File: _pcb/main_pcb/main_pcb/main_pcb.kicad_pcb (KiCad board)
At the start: 2 copper layers, 160 x 110 mm, 6 parts, among them U1 Pico, U2 74HC4051

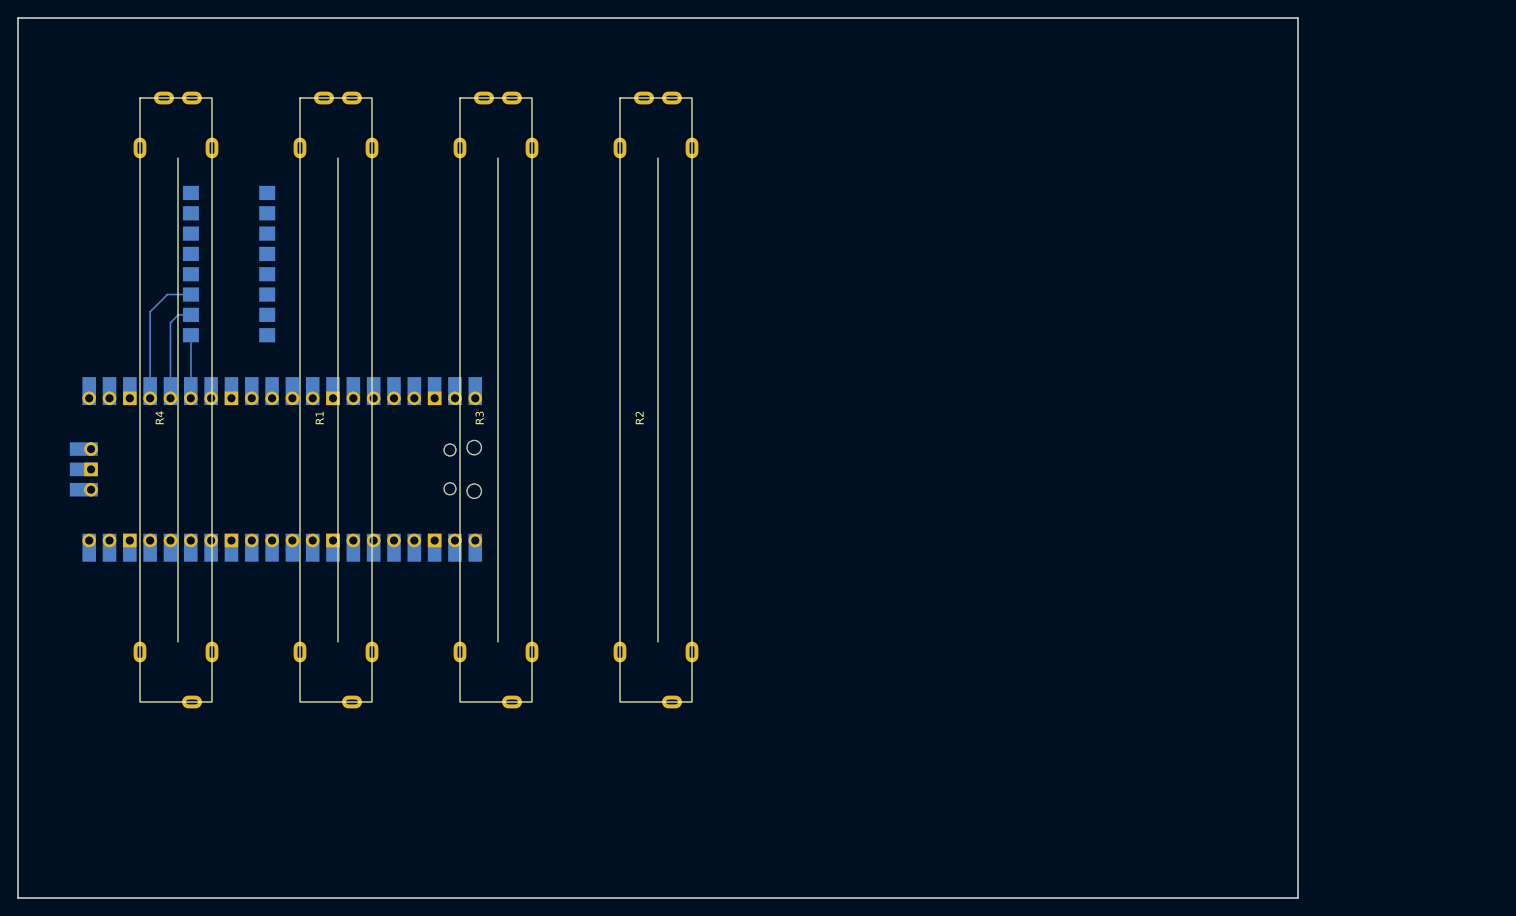
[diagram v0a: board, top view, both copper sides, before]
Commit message: for now the last commit for pcb as buying pcb is too expensive
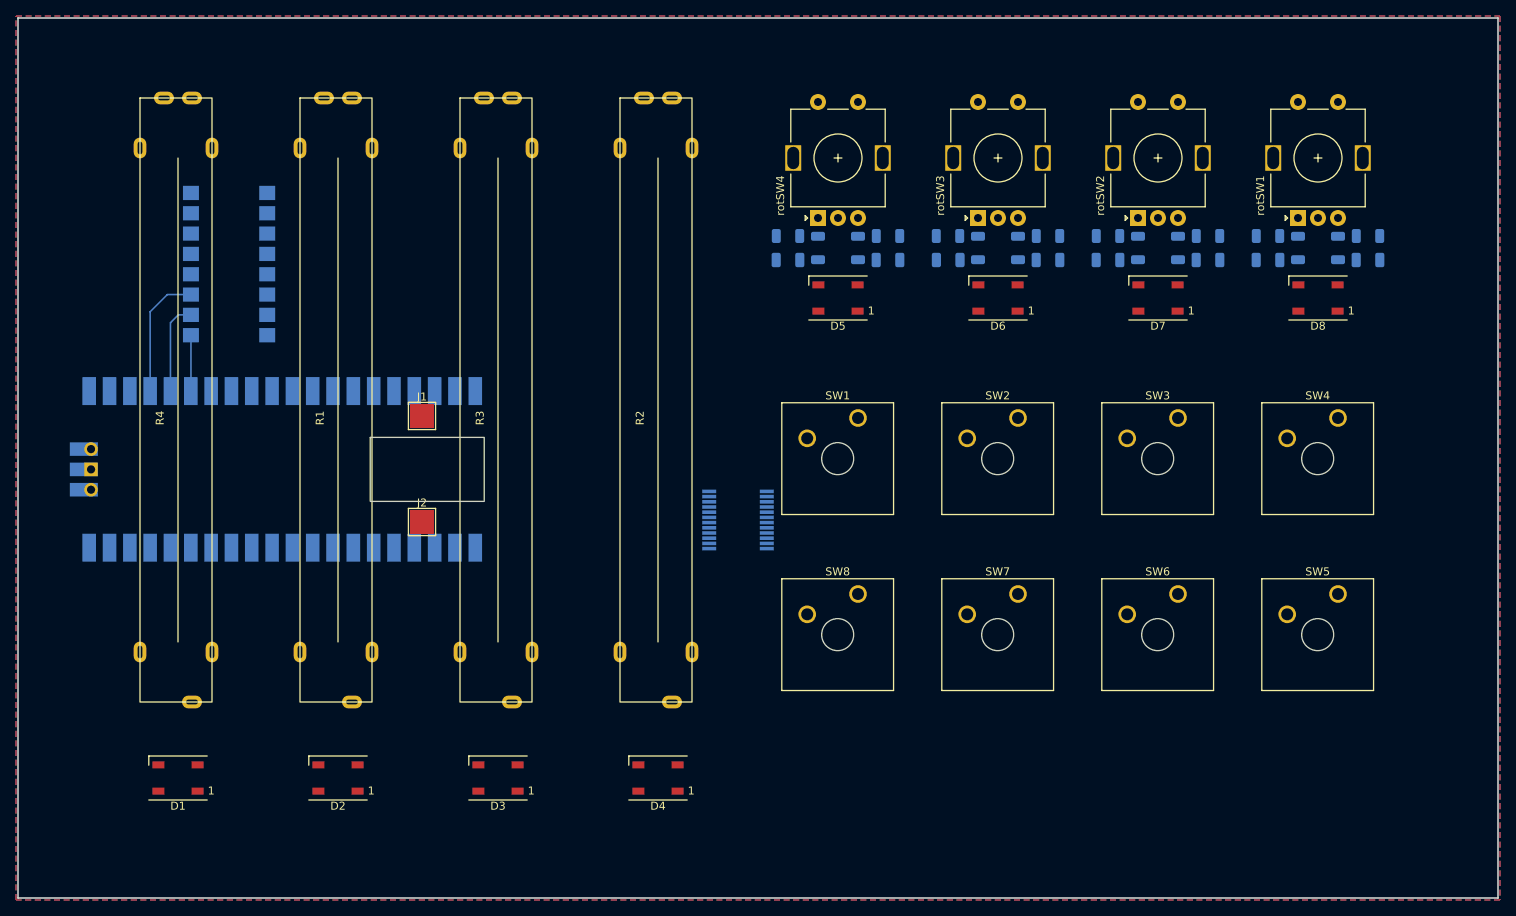
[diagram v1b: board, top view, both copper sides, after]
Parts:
- added C1: C, Capacitor_SMD:C_1206_3216Metric, B.Cu at (188.8, 80.2)
- added C2: C, Capacitor_SMD:C_1206_3216Metric, B.Cu at (176.2, 80.2)
- added C3: C, Capacitor_SMD:C_1206_3216Metric, B.Cu at (156.2, 80.2)
- added C4: C, Capacitor_SMD:C_1206_3216Metric, B.Cu at (168.8, 80.2)
- added C5: C, Capacitor_SMD:C_1206_3216Metric, B.Cu at (136.3, 80.2)
- added C6: C, Capacitor_SMD:C_1206_3216Metric, B.Cu at (148.8, 80.2)
- added C7: C, Capacitor_SMD:C_1206_3216Metric, B.Cu at (116.2, 80.2)
- added C8: C, Capacitor_SMD:C_1206_3216Metric, B.Cu at (128.8, 80.2)
- added D1: WS2812B, LED_SMD:LED_WS2812B_PLCC4_5.0x5.0mm_P3.2mm, F.Cu at (40.0, 145.0)
- added D2: WS2812B, LED_SMD:LED_WS2812B_PLCC4_5.0x5.0mm_P3.2mm, F.Cu at (60.0, 145.0)
- added D3: WS2812B, LED_SMD:LED_WS2812B_PLCC4_5.0x5.0mm_P3.2mm, F.Cu at (80.0, 145.0)
- added D4: WS2812B, LED_SMD:LED_WS2812B_PLCC4_5.0x5.0mm_P3.2mm, F.Cu at (100.0, 145.0)
- added D5: WS2812B, LED_SMD:LED_WS2812B_PLCC4_5.0x5.0mm_P3.2mm, F.Cu at (122.5, 85.0)
- added D6: WS2812B, LED_SMD:LED_WS2812B_PLCC4_5.0x5.0mm_P3.2mm, F.Cu at (142.5, 85.0)
- added D7: WS2812B, LED_SMD:LED_WS2812B_PLCC4_5.0x5.0mm_P3.2mm, F.Cu at (162.5, 85.0)
- added D8: WS2812B, LED_SMD:LED_WS2812B_PLCC4_5.0x5.0mm_P3.2mm, F.Cu at (182.5, 85.0)
- added J1: Conn_01x01_Pin, TestPoint:TestPoint_Pad_3.0x3.0mm, F.Cu at (70.5, 99.8)
- added J2: Conn_01x01_Pin, TestPoint:TestPoint_Pad_3.0x3.0mm, F.Cu at (70.5, 113.0)
- added R10: R, Resistor_SMD:R_1206_3216Metric, B.Cu at (165.0, 78.8)
- added R11: R, Resistor_SMD:R_1206_3216Metric, B.Cu at (156.2, 77.2)
- added R12: R, Resistor_SMD:R_1206_3216Metric, B.Cu at (168.8, 77.2)
- added R13: R, Resistor_SMD:R_1206_3216Metric, B.Cu at (140.0, 78.8)
- added R14: R, Resistor_SMD:R_1206_3216Metric, B.Cu at (145.0, 78.8)
- added R15: R, Resistor_SMD:R_1206_3216Metric, B.Cu at (136.2, 77.2)
- added R16: R, Resistor_SMD:R_1206_3216Metric, B.Cu at (148.8, 77.2)
- added R17: R, Resistor_SMD:R_1206_3216Metric, B.Cu at (120.0, 78.8)
- added R18: R, Resistor_SMD:R_1206_3216Metric, B.Cu at (125.0, 78.8)
- added R19: R, Resistor_SMD:R_1206_3216Metric, B.Cu at (116.2, 77.2)
- added R20: R, Resistor_SMD:R_1206_3216Metric, B.Cu at (128.8, 77.2)
- added R5: R, Resistor_SMD:R_1206_3216Metric, B.Cu at (185.0, 78.8)
- added R6: R, Resistor_SMD:R_1206_3216Metric, B.Cu at (180.0, 78.8)
- added R7: R, Resistor_SMD:R_1206_3216Metric, B.Cu at (176.2, 77.2)
- added R8: R, Resistor_SMD:R_1206_3216Metric, B.Cu at (188.8, 77.2)
- added R9: R, Resistor_SMD:R_1206_3216Metric, B.Cu at (160.0, 78.8)
- added SW1: SW_Push, Button_Switch_Keyboard:SW_Cherry_MX_1.00u_Plate, F.Cu at (125.0, 100.0)
- added SW2: SW_Push, Button_Switch_Keyboard:SW_Cherry_MX_1.00u_Plate, F.Cu at (145.0, 100.0)
- added SW3: SW_Push, Button_Switch_Keyboard:SW_Cherry_MX_1.00u_Plate, F.Cu at (165.0, 100.0)
- added SW4: SW_Push, Button_Switch_Keyboard:SW_Cherry_MX_1.00u_Plate, F.Cu at (185.0, 100.0)
- added SW5: SW_Push, Button_Switch_Keyboard:SW_Cherry_MX_1.00u_Plate, F.Cu at (185.0, 122.0)
- added SW6: SW_Push, Button_Switch_Keyboard:SW_Cherry_MX_1.00u_Plate, F.Cu at (165.0, 122.0)
- added SW7: SW_Push, Button_Switch_Keyboard:SW_Cherry_MX_1.00u_Plate, F.Cu at (145.0, 122.0)
- added SW8: SW_Push, Button_Switch_Keyboard:SW_Cherry_MX_1.00u_Plate, F.Cu at (125.0, 122.0)
- added U3: PCF8575DBR, Package_SO:SSOP-24_5.3x8.2mm_P0.65mm, B.Cu at (110.0, 112.8)
- added rotSW1: RotaryEncoder_Switch, Rotary_Encoder:RotaryEncoder_Alps_EC11E-Switch_Vertical_H20mm, F.Cu at (182.5, 67.5)
- added rotSW2: RotaryEncoder_Switch, Rotary_Encoder:RotaryEncoder_Alps_EC11E-Switch_Vertical_H20mm, F.Cu at (162.5, 67.5)
- added rotSW3: RotaryEncoder_Switch, Rotary_Encoder:RotaryEncoder_Alps_EC11E-Switch_Vertical_H20mm, F.Cu at (142.5, 67.5)
- added rotSW4: RotaryEncoder_Switch, Rotary_Encoder:RotaryEncoder_Alps_EC11E-Switch_Vertical_H20mm, F.Cu at (122.5, 67.5)
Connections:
- R1 pad 1: Net-(R1-Pad1) -> 3.3 V
- R1 pad 3: Net-(R1-Pad3) -> GND
- R2 pad 1: Net-(R1-Pad1) -> 3.3 V
- R2 pad 3: Net-(R1-Pad3) -> GND
- R3 pad 1: Net-(R1-Pad1) -> 3.3 V
- R3 pad 3: Net-(R1-Pad3) -> GND
- R4 pad 1: Net-(R1-Pad1) -> 3.3 V
- R4 pad 3: Net-(R1-Pad3) -> GND
- U1 pad 10: unconnected-(U1-GPIO7-Pad10) -> Rotary_SW_Button_2
- U1 pad 11: unconnected-(U1-GPIO8-Pad11) -> Rotary_SW_CLK_3
- U1 pad 12: unconnected-(U1-GPIO9-Pad12) -> Rotary_SW_DATA_3
- U1 pad 14: unconnected-(U1-GPIO10-Pad14) -> Rotary_SW_Button_3
- U1 pad 15: unconnected-(U1-GPIO11-Pad15) -> Rotary_SW_CLK_4
- U1 pad 16: unconnected-(U1-GPIO12-Pad16) -> Rotary_SW_DATA_4
- U1 pad 17: unconnected-(U1-GPIO13-Pad17) -> Rotary_SW_Button_4
- U1 pad 18: unconnected-(U1-GND-Pad18) -> GND
- U1 pad 20: unconnected-(U1-GPIO15-Pad20) -> IO_EXPANDER_INT
- U1 pad 21: unconnected-(U1-GPIO16-Pad21) -> IO_EXPANDER_SDA
- U1 pad 22: unconnected-(U1-GPIO17-Pad22) -> IO_EXPANDER_SCL
- U1 pad 29: unconnected-(U1-GPIO22-Pad29) -> WS2812_GPIO
- U1 pad 4: unconnected-(U1-GPIO2-Pad4) -> Rotary_SW_CLK_1
- U1 pad 5: unconnected-(U1-GPIO3-Pad5) -> Rotary_SW_DATA_1
- U1 pad 6: unconnected-(U1-GPIO4-Pad6) -> Rotary_SW_Button_1
- U1 pad 7: unconnected-(U1-GPIO5-Pad7) -> Rotary_SW_CLK_2
- U1 pad 9: unconnected-(U1-GPIO6-Pad9) -> Rotary_SW_DATA_2
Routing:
- added copper zone on B.Cu, net GND
- added copper zone on F.Cu, net GND
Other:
- board size 160 x 110 mm -> 185 x 110 mm
